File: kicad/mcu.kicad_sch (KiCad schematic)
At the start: 27 parts

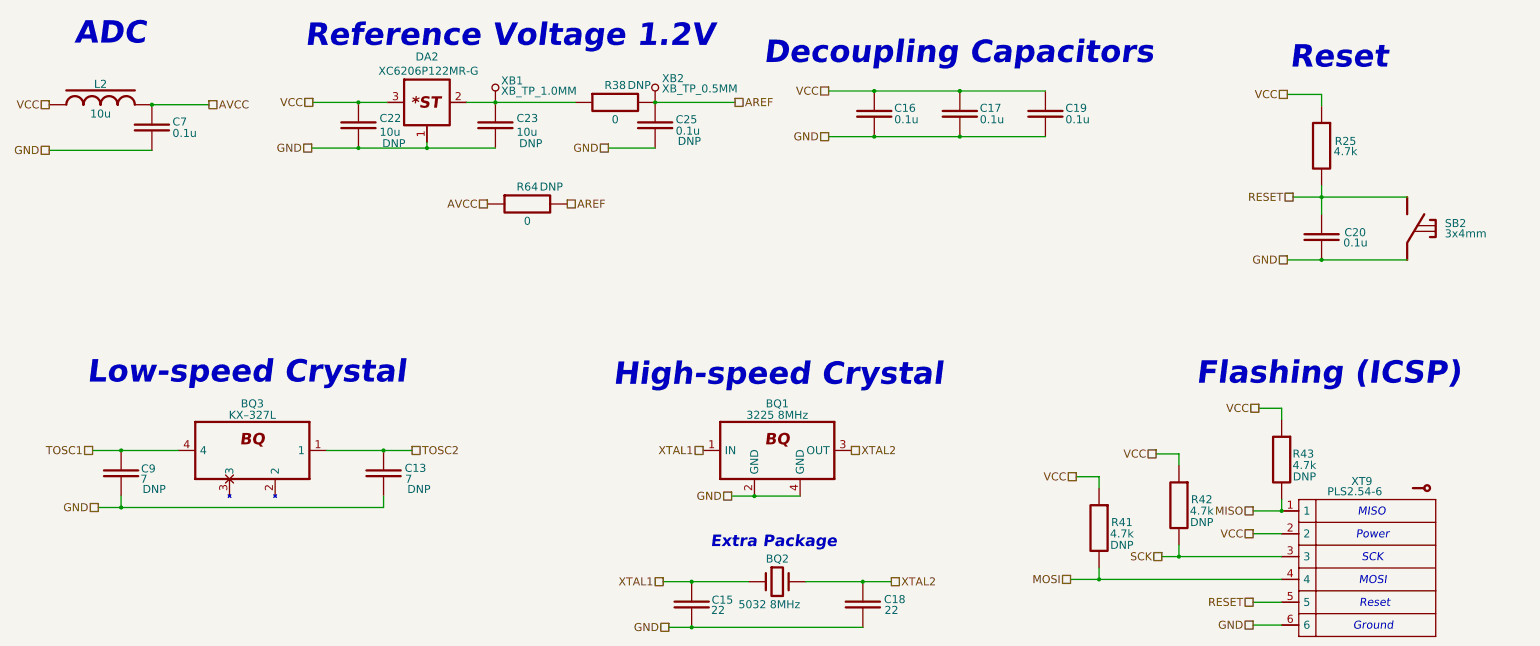
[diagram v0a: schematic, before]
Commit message: Reannotate schematic; Fix 5032 crystal footprint field; Update PCB with 5032 crystal
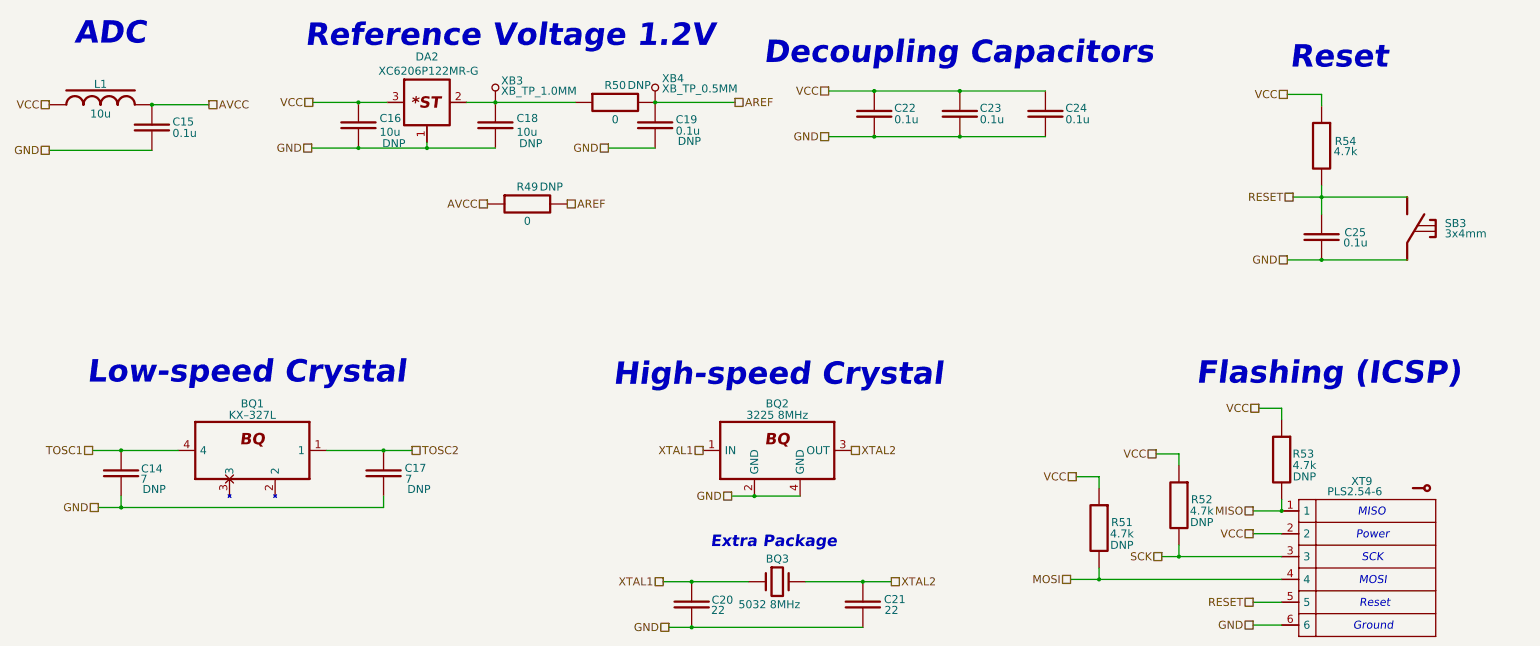
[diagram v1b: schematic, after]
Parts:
- BQ3: renamed from BQ2; footprint (none) -> Crystal:Crystal_SMD_5032-2Pin_5.0x3.2mm
- renumbered BQ3 to BQ1, BQ1 to BQ2, C9 to C14, C7 to C15, C22 to C16, C13 to C17, C23 to C18, C25 to C19, C15 to C20, C18 to C21, C16 to C22, C17 to C23, C19 to C24, C20 to C25, L2 to L1, R64 to R49, R38 to R50, R41 to R51, R42 to R52, R43 to R53, R25 to R54, SB2 to SB3, XB1 to XB3, XB2 to XB4
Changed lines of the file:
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@@
   (symbol (lib_id "Capacitors:C_CAP") (at 238.252 96.52 270) (unit 1)
     (in_bom yes) (on_board yes)
-    (property "Reference" "C16" (id 0) (at 242.697 95.25 90)
+    (property "Reference" "C22" (id 0) (at 242.697 95.25 90)
       (effects (font (size 1.778 1.778)) (justify left))
     )
@@
   (symbol (lib_id "Capacitors:C_CAP") (at 70.612 176.53 270) (unit 1)
     (in_bom yes) (on_board yes)
-    (property "Reference" "C9" (id 0) (at 75.057 175.514 90)
+    (property "Reference" "C14" (id 0) (at 75.057 175.514 90)
       (effects (font (size 1.778 1.778)) (justify left))
     )
@@
   (symbol (lib_id "Resistors:R_RES") (at 337.82 103.632 270) (unit 1)
     (in_bom yes) (on_board yes)
-    (property "Reference" "R25" (id 0) (at 343.154 102.616 90)
+    (property "Reference" "R54" (id 0) (at 343.154 102.616 90)
       (effects (font (size 1.778 1.778)))
     )
@@
   (symbol (lib_id "Capacitors:C_CAP") (at 276.352 96.52 270) (mirror x) (unit 1)
     (in_bom yes) (on_board yes)
-    (property "Reference" "C19" (id 0) (at 280.797 95.25 90)
+    (property "Reference" "C24" (id 0) (at 280.797 95.25 90)
       (effects (font (size 1.778 1.778)) (justify left))
     )
@@
   (symbol (lib_id "Connectors:XB_TP_1.0MM") (at 153.924 93.98 0) (unit 1)
     (in_bom no) (on_board yes)
-    (property "Reference" "XB1" (id 0) (at 155.194 89.154 0)
+    (property "Reference" "XB3" (id 0) (at 155.194 89.154 0)
       (effects (font (size 1.778 1.778)) (justify left))
     )
@@
   (symbol (lib_id "Switches:SB_ON") (at 356.87 121.412 270) (mirror x) (unit 1)
     (in_bom yes) (on_board yes)
-    (property "Reference" "SB2" (id 0) (at 365.252 120.904 90)
+    (property "Reference" "SB3" (id 0) (at 365.252 120.904 90)
       (effects (font (size 1.778 1.778)) (justify left))
     )
@@
   (symbol (lib_id "Capacitors:C_CAP") (at 235.712 205.74 270) (unit 1)
     (in_bom yes) (on_board yes)
-    (property "Reference" "C18" (id 0) (at 240.411 204.597 90)
+    (property "Reference" "C21" (id 0) (at 240.411 204.597 90)
       (effects (font (size 1.778 1.778)) (justify left))
     )
@@
   (symbol (lib_id "Misc:BQ_QUARTZ") (at 216.662 200.66 0) (unit 1)
     (in_bom yes) (on_board yes)
-    (property "Reference" "BQ2" (id 0) (at 214.122 195.58 0)
+    (property "Reference" "BQ3" (id 0) (at 214.122 195.58 0)
       (effects (font (size 1.778 1.778)) (justify left))
     )
@@
       (effects (font (size 1.778 1.778)) (justify left))
     )
-    (property "Footprint" "" (id 2) (at 216.662 200.66 0)
+    (property "Footprint" "Crystal:Crystal_SMD_5032-2Pin_5.0x3.2mm" (id 2) (at 216.662 200.66 0)
       (effects (font (size 1.778 1.778)) hide)
     )
@@
   (symbol (lib_id "Resistors:R_RES") (at 306.07 183.642 270) (unit 1)
     (in_bom yes) (on_board yes)
-    (property "Reference" "R42" (id 0) (at 311.15 182.372 90)
+    (property "Reference" "R52" (id 0) (at 311.15 182.372 90)
       (effects (font (size 1.778 1.778)))
     )
@@
   (symbol (lib_id "Capacitors:C_CAP") (at 77.47 99.568 270) (mirror x) (unit 1)
     (in_bom yes) (on_board yes)
-    (property "Reference" "C7" (id 0) (at 82.042 98.298 90)
+    (property "Reference" "C15" (id 0) (at 82.042 98.298 90)
       (effects (font (size 1.778 1.778)) (justify left))
     )
@@
   (symbol (lib_id "Resistors:R_RES") (at 328.93 173.482 270) (unit 1)
     (in_bom yes) (on_board yes)
-    (property "Reference" "R43" (id 0) (at 333.756 172.212 90)
+    (property "Reference" "R53" (id 0) (at 333.756 172.212 90)
       (effects (font (size 1.778 1.778)))
     )
@@
   (symbol (lib_id "Resistors:R_RES") (at 288.29 188.722 270) (unit 1)
     (in_bom yes) (on_board yes)
-    (property "Reference" "R41" (id 0) (at 293.37 187.452 90)
+    (property "Reference" "R51" (id 0) (at 293.37 187.452 90)
       (effects (font (size 1.778 1.778)))
     )
@@
   (symbol (lib_id "Capacitors:C_CAP") (at 123.444 99.06 270) (unit 1)
     (in_bom yes) (on_board yes)
-    (property "Reference" "C22" (id 0) (at 128.143 97.5106 90)
+    (property "Reference" "C16" (id 0) (at 128.143 97.5106 90)
       (effects (font (size 1.778 1.778)) (justify left))
     )
@@
   (symbol (lib_id "Capacitors:C_CAP") (at 153.924 99.06 270) (unit 1)
     (in_bom yes) (on_board yes)
-    (property "Reference" "C23" (id 0) (at 158.623 97.5106 90)
+    (property "Reference" "C18" (id 0) (at 158.623 97.5106 90)
       (effects (font (size 1.778 1.778)) (justify left))
     )
@@
   (symbol (lib_id "Power:POWER") (at 77.47 94.488 0) (unit 1)
     (in_bom yes) (on_board yes) (fields_autoplaced)
-    (property "Reference" "#PWR0127" (id 0) (at 77.47 97.028 0)
+    (property "Reference" "#PWR032" (id 0) (at 77.47 97.028 0)
       (effects (font (size 1.778 1.778)) hide)
     )
@@
   (symbol (lib_id "Inductors:L_FERR") (at 66.04 94.488 0) (unit 1)
     (in_bom yes) (on_board yes)
-    (property "Reference" "L2" (id 0) (at 66.04 89.916 0)
+    (property "Reference" "L1" (id 0) (at 66.04 89.916 0)
       (effects (font (size 1.778 1.778)))
     )
@@
   (symbol (lib_id "Capacitors:C_CAP") (at 257.302 96.52 270) (unit 1)
     (in_bom yes) (on_board yes)
-    (property "Reference" "C17" (id 0) (at 261.747 95.25 90)
+    (property "Reference" "C23" (id 0) (at 261.747 95.25 90)
       (effects (font (size 1.778 1.778)) (justify left))
     )
@@
   (symbol (lib_id "Resistors:R_RES") (at 161.036 116.586 0) (unit 1)
     (in_bom yes) (on_board yes)
-    (property "Reference" "R64" (id 0) (at 161.036 112.776 0)
+    (property "Reference" "R49" (id 0) (at 161.036 112.776 0)
       (effects (font (size 1.778 1.778)))
     )
@@
   (symbol (lib_id "Connectors:XB_TP_0.5MM") (at 189.484 93.98 0) (unit 1)
     (in_bom no) (on_board yes)
-    (property "Reference" "XB2" (id 0) (at 191.008 88.646 0)
+    (property "Reference" "XB4" (id 0) (at 191.008 88.646 0)
       (effects (font (size 1.778 1.778)) (justify left))
     )
@@
   (symbol (lib_id "Capacitors:C_CAP") (at 337.82 123.952 270) (unit 1)
     (in_bom yes) (on_board yes)
-    (property "Reference" "C20" (id 0) (at 342.9 122.936 90)
+    (property "Reference" "C25" (id 0) (at 342.9 122.936 90)
       (effects (font (size 1.778 1.778)) (justify left))
     )
@@
   (symbol (lib_id "Chips:Crystal_4PIN") (at 216.662 175.26 0) (unit 1)
     (in_bom yes) (on_board yes)
-    (property "Reference" "BQ1" (id 0) (at 216.662 161.036 0)
+    (property "Reference" "BQ2" (id 0) (at 216.662 161.036 0)
       (effects (font (size 1.778 1.778)))
     )
@@
   (symbol (lib_id "Capacitors:C_CAP") (at 197.612 205.74 270) (unit 1)
     (in_bom yes) (on_board yes)
-    (property "Reference" "C15" (id 0) (at 202.057 204.724 90)
+    (property "Reference" "C20" (id 0) (at 202.057 204.724 90)
       (effects (font (size 1.778 1.778)) (justify left))
     )
@@
   (symbol (lib_id "Capacitors:C_CAP") (at 189.484 99.06 270) (mirror x) (unit 1)
     (in_bom yes) (on_board yes)
-    (property "Reference" "C25" (id 0) (at 194.056 97.79 90)
+    (property "Reference" "C19" (id 0) (at 194.056 97.79 90)
       (effects (font (size 1.778 1.778)) (justify left))
     )
@@
   (symbol (lib_id "Capacitors:C_CAP") (at 129.032 176.53 270) (unit 1)
     (in_bom yes) (on_board yes)
-    (property "Reference" "C13" (id 0) (at 133.731 175.387 90)
+    (property "Reference" "C17" (id 0) (at 133.731 175.387 90)
       (effects (font (size 1.778 1.778)) (justify left))
     )
@@
   (symbol (lib_id "Chips:KX–327L") (at 99.822 175.26 0) (mirror y) (unit 1)
     (in_bom yes) (on_board yes)
-    (property "Reference" "BQ3" (id 0) (at 99.822 161.036 0)
+    (property "Reference" "BQ1" (id 0) (at 99.822 161.036 0)
       (effects (font (size 1.778 1.778)))
     )
@@
   (symbol (lib_id "Resistors:R_RES") (at 180.594 93.98 0) (unit 1)
     (in_bom yes) (on_board yes)
-    (property "Reference" "R38" (id 0) (at 180.594 90.17 0)
-      (effects (font (size 1.778 1.778)))
-    )
+    (property "Reference" "R50" (id 0) (at 180.594 90.17 0)
+      (effects (font (size 1.778 1.778)))
+    )

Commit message: Add voltage value to caps, update BOM, SCH, ASM
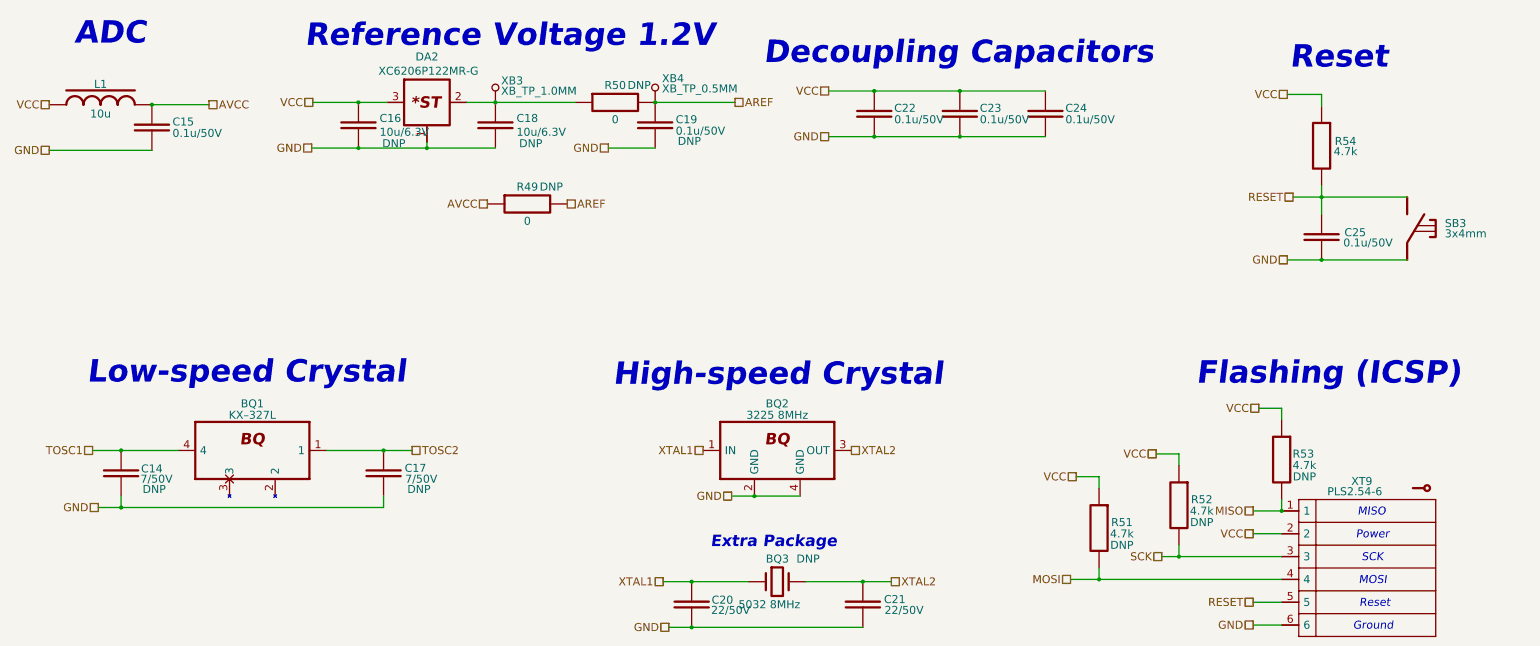
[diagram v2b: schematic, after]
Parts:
- BQ3: Assembly (none) -> DNP
- C14, C17: value 7 -> 7/50V; Case/Package (none) -> 0603; Tolerance (none) -> ±10%; Type (none) -> X7R
- C15, C19, C22, C23, C24, C25: value 0.1u -> 0.1u/50V; Tolerance (none) -> ±10%; Type (none) -> X7R
- C16, C18: value 10u -> 10u/6.3V; Case/Package (none) -> 0603; Tolerance (none) -> ±10%; Type (none) -> X7R
- C20, C21: value 22 -> 22/50V; Case/Package (none) -> 0603; Tolerance (none) -> ±10%; Type (none) -> X7R
- R49, R50, R51, R52, R53, R54: Case/Package 0000 -> 0603; Tolerance ±% -> ±5%

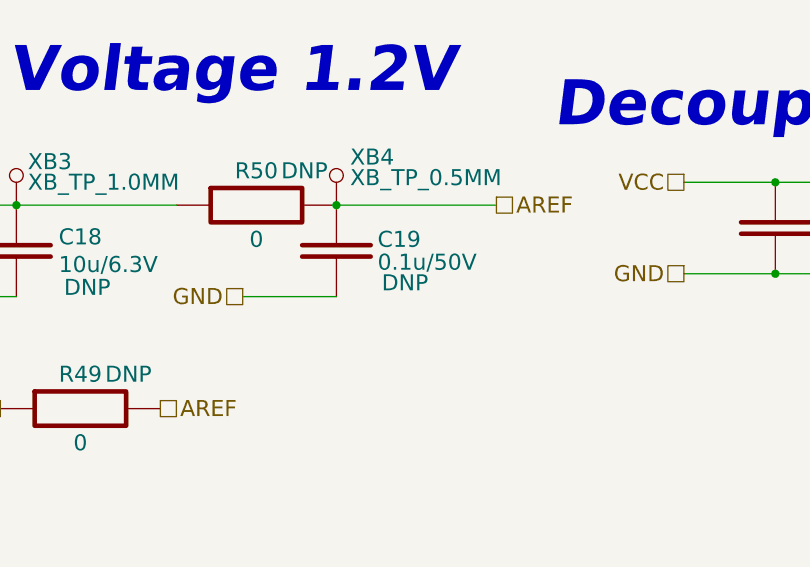
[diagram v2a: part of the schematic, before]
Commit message: Add docs; Update values of components according to PCB
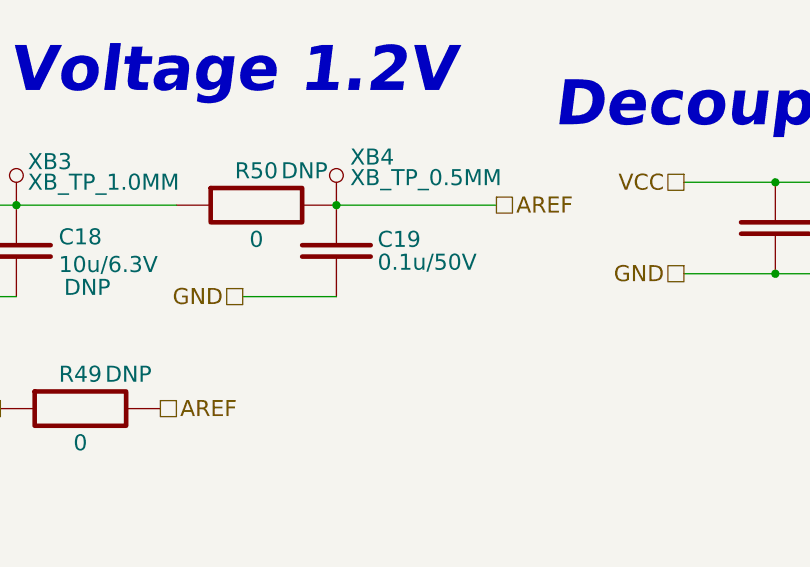
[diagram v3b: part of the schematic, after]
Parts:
- C19: Assembly DNP -> (none)
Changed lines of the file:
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@@
       (effects (font (size 1.778 1.778)) hide)
     )
-    (property "Assembly" "DNP" (id 4) (at 197.104 102.616 90)
+    (property "Assembly" "" (id 4) (at 197.104 102.616 90)
       (effects (font (size 1.778 1.778)))
     )

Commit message: Add wiring diagram; Add work ours (stage 2); refactor folders
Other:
- title: (none) -> RadioSens v1
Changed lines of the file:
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@@
 (kicad_sch (version 20211123) (generator eeschema)
   (paper "A3")
+  (title_block
+    (title "RadioSens v1")
+    (comment 2 "Electrical Circuit")
+  )
   (junction (at 70.612 184.15) (diameter 0) (color 0 0 0 0)
   )

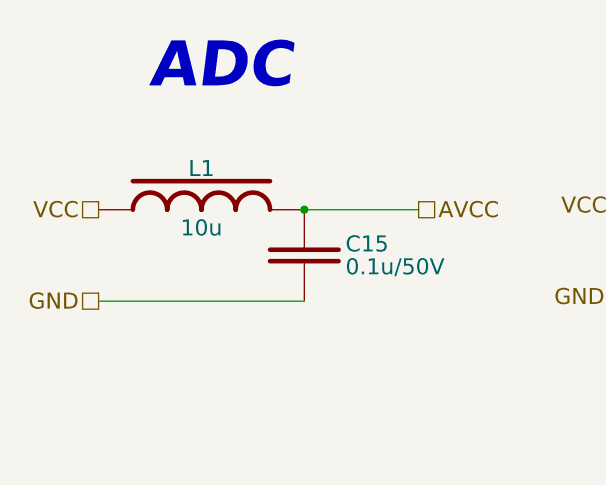
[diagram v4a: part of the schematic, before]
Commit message: update: to 7.0 ver and add fiducials
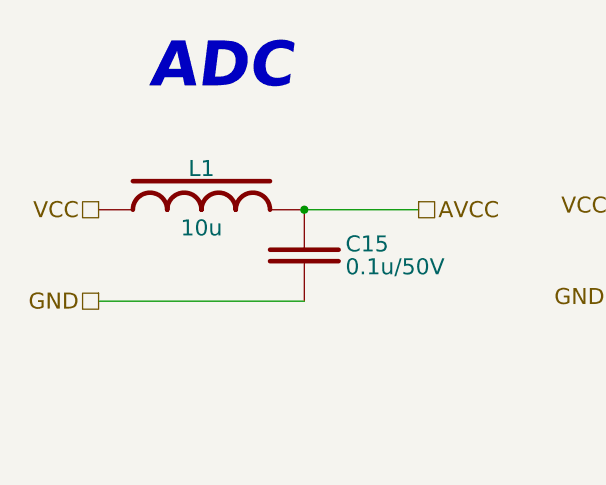
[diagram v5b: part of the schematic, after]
